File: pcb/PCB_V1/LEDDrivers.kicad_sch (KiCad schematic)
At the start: 50 parts, among them J711 LED +/- (return isolated), J721 LED +/- (return isolated), J731 LED +/- (return isolated), Q711 CSD19534Q5A, Q721 CSD19538Q3A, U700 SN74LVC1G08DBVR, U710 AL8853S-13, U720 AL8853S-13

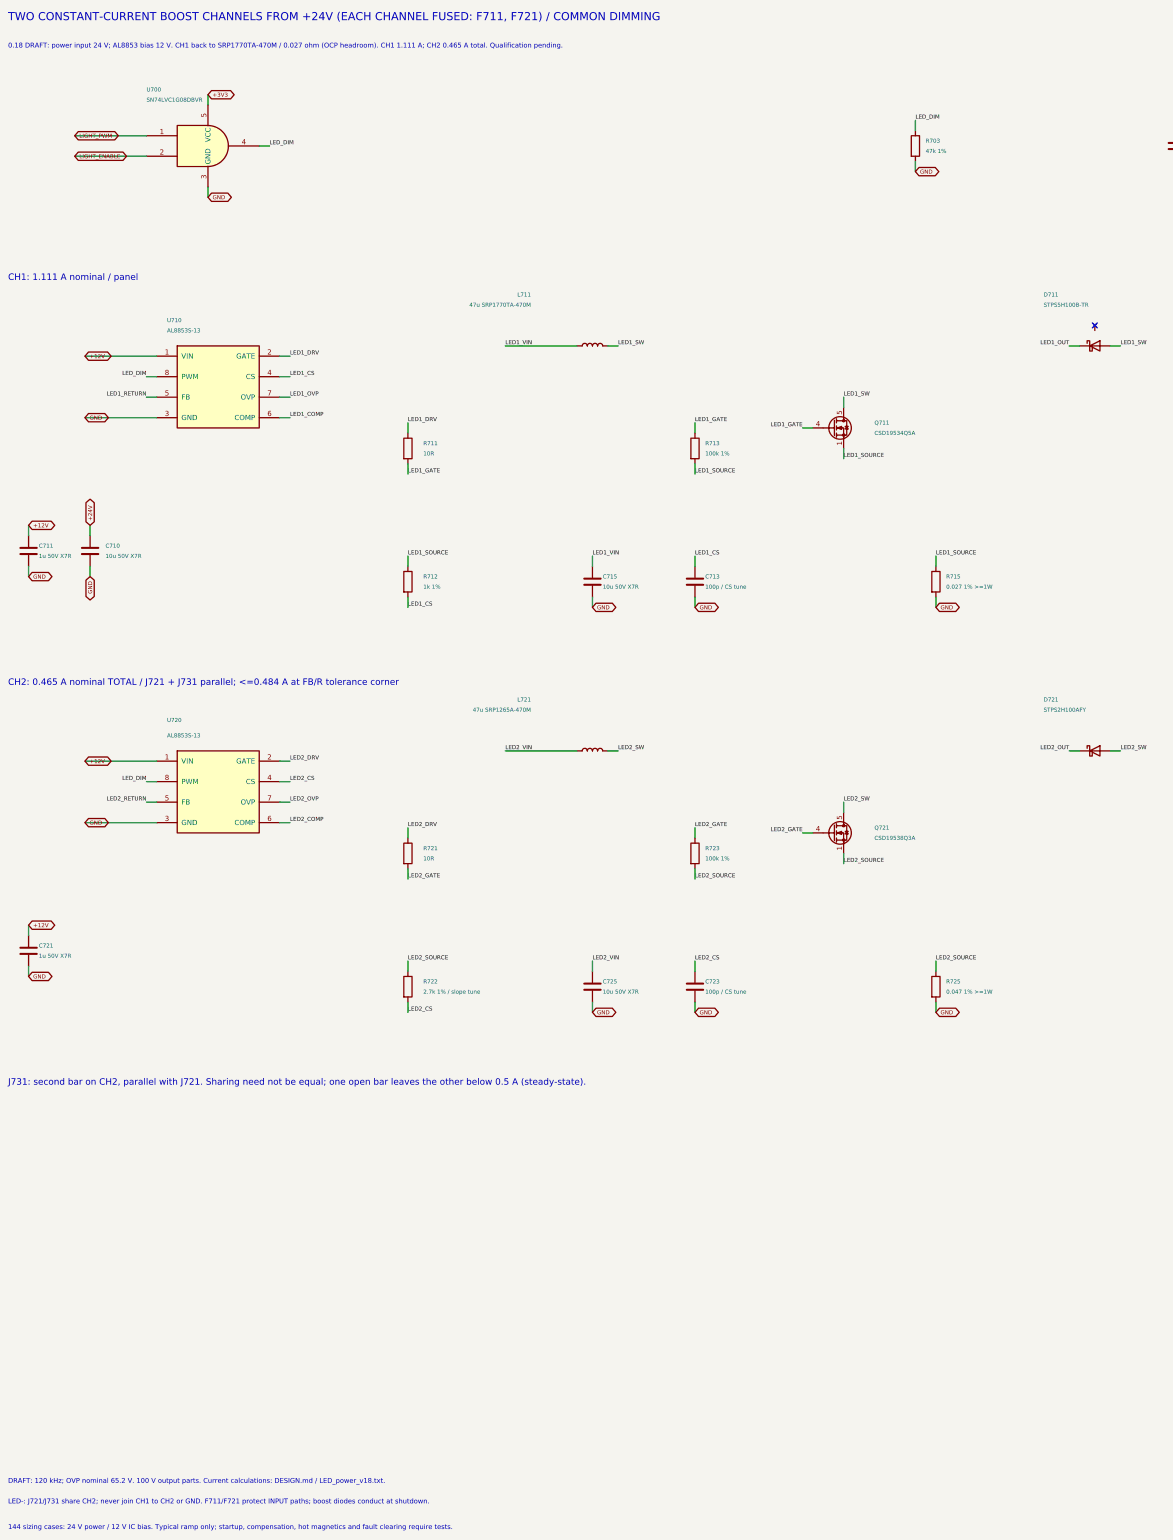
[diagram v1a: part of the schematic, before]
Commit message: pcb: revision 0.20 cost-down with new footprints and placement
- RTC: DS3231MZ replaced by NXP PCF8563T/5 with an Epson FC-135 crystal
  (CL 12.5 pF), C304 18 pF C0G on OSCI, BAT54C supply OR (D303) and R307
  1k from the CR2032.
- Boost switches Q711/Q721: AOS AOD66923 (DPAK) on a project footprint
  that keeps the S1/2/3 G4 D5 numbering; diodes D711/D721: Vishay SS5P10
  (TO-277A).
- L101 cjiang FXL0630-100-M and L902 PROD PSPMAA0604-220M-ANP on the
  KiCad FXL0630 land.
- LED switch areas and the RTC cluster re-placed (29 parts moved);
  ERC 0, DRC 0, 340 unrouted links.
- Checks, price/JLC snapshots v20, reports, placement images and docs
  updated: USD 31.62 per board (29.52 for five boards).

Co-Authored-By: Claude Opus 5.5 <noreply@anthropic.com>
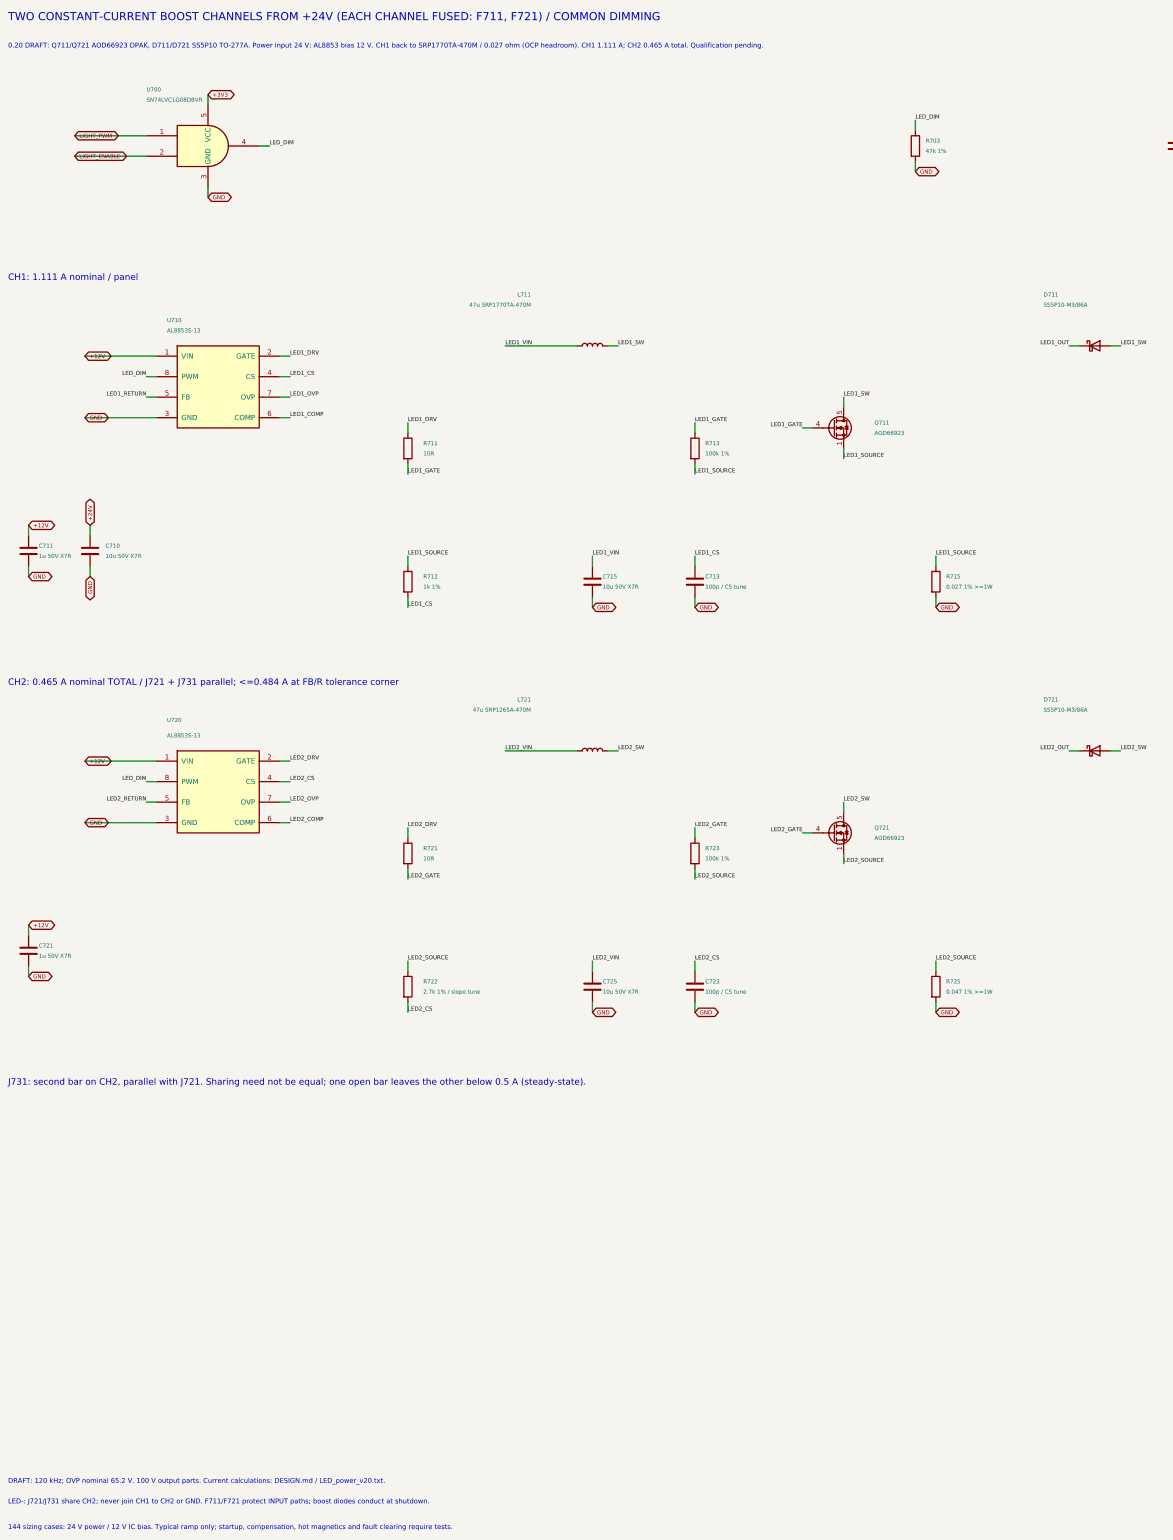
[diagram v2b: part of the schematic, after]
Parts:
- D711: value STPS5H100B-TR -> SS5P10-M3/86A; footprint Package_TO_SOT_SMD:TO-252-2 -> GrowBox:Vishay_TO-277A_D_K1_A2; symbol GrowBox:STPS5H100B -> Device:D_Schottky; LCSC C10648 -> C46986; MPN STPS5H100B-TR -> SS5P10-M3/86A; Manufacturer STMicroelectronics -> Vishay
- D721: value STPS2H100AFY -> SS5P10-M3/86A; footprint Diode_SMD:D_SOD-128 -> GrowBox:Vishay_TO-277A_D_K1_A2; LCSC C3757915 -> C46986; MPN STPS2H100AFY -> SS5P10-M3/86A; Manufacturer STMicroelectronics -> Vishay
- Q711: value CSD19534Q5A -> AOD66923; footprint GrowBox:TI_DQJ0008A_CSD19534Q5A -> GrowBox:TO-252-2_NMOS_S123_G4_D5; symbol GrowBox:CSD19534Q5A -> GrowBox:AOD66923; LCSC C114200 -> C485687; MPN CSD19534Q5A -> AOD66923; Manufacturer Texas Instruments -> AOS
- Q721: value CSD19538Q3A -> AOD66923; footprint GrowBox:TI_DNH0008A_CSD19538Q3A -> GrowBox:TO-252-2_NMOS_S123_G4_D5; symbol GrowBox:CSD19538Q3A -> GrowBox:AOD66923; LCSC (none) -> C485687; MPN (none) -> AOD66923; Manufacturer (none) -> AOS
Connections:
- net LED1_OUT: now also D711.1 (K); no longer D711.2 (K)
- net LED1_SW: now also D711.2 (A); no longer D711.3 (A)
- no-connect marks 1 -> 0
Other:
- note added: "0.20 DRAFT: Q711/Q721 AOD66923 DPAK, D711/D721 SS5P10 TO-277A. Power input 24 V; AL8853 bias 12 V. CH1 back to SRP1770TA-470M / 0.027 ohm (OCP headroom). CH1 1.111 A; CH2 0.465 A total. Qualification pending."
- note added: "DRAFT: 120 kHz; OVP nominal 65.2 V. 100 V output parts. Current calculations: DESIGN.md / LED_power_v20.txt."
- note removed: "0.18 DRAFT: power input 24 V; AL8853 bias 12 V. CH1 back to SRP1770TA-470M / 0.027 ohm (OCP headroom). CH1 1.111 A; CH2 0.465 A total. Qualification pending."
- note removed: "DRAFT: 120 kHz; OVP nominal 65.2 V. 100 V output parts. Current calculations: DESIGN.md / LED_power_v18.txt."
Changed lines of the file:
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@@
 		(title "07 - AL8853 LED drivers, 24 V input, 2 channels")
 		(date "2026-09-29")
-		(rev "0.18-DRAFT")
+		(rev "0.20-DRAFT")
 		(company "GrowBox controller")
 		(comment 1 "Simplified prototype; unrouted; hardware qualification pending")
@@
 		)
 	)
-	(text "DRAFT: 120 kHz; OVP nominal 65.2 V. 100 V output parts. Current calculations: DESIGN.md / LED_power_v18.txt."
+	(text "DRAFT: 120 kHz; OVP nominal 65.2 V. 100 V output parts. Current calculations: DESIGN.md / LED_power_v20.txt."
 		(exclude_from_sim no)
 		(at 20.32 378.46 0)
@@
 		)
 	)
-	(text "0.18 DRAFT: power input 24 V; AL8853 bias 12 V. CH1 back to SRP1770TA-470M / 0.027 ohm (OCP headroom). CH1 1.111 A; CH2 0.465 A total. Qualification pending."
+	(text "0.20 DRAFT: Q711/Q721 AOD66923 DPAK, D711/D721 SS5P10 TO-277A. Power input 24 V; AL8853 bias 12 V. CH1 back to SRP1770TA-470M / 0.027 ohm (OCP headroom). CH1 1.111 A; CH2 0.465 A total. Qualification pending."
 		(exclude_from_sim no)
 		(at 20.32 22.86 0)
@@
 			)
 		)
-		(property "Value" "STPS2H100AFY"
+		(property "Value" "SS5P10-M3/86A"
 			(at 276.86 187.96 0)
 			(show_name no)
@@
 			)
 		)
-		(property "Footprint" "Diode_SMD:D_SOD-128"
+		(property "Footprint" "GrowBox:Vishay_TO-277A_D_K1_A2"
 			(at 289.56 198.12 0)
 			(hide yes)
@@
 			)
 		)
-		(property "Datasheet" "https://www.st.com/resource/en/datasheet/stps2h100-y.pdf"
+		(property "Datasheet" "https://www.vishay.com/docs/88984/ss5p10.pdf"
 			(at 289.56 198.12 0)
 			(hide yes)
@@
 			)
 		)
-		(property "Manufacturer" "STMicroelectronics"
+		(property "Manufacturer" "Vishay"
 			(at 289.56 198.12 0)
 			(hide yes)
@@
 			)
 		)
-		(property "MPN" "STPS2H100AFY"
+		(property "MPN" "SS5P10-M3/86A"
 			(at 289.56 198.12 0)
 			(hide yes)
@@
 			)
 		)
-		(property "LCSC" "C3757915"
+		(property "LCSC" "C46986"
 			(at 289.56 198.12 0)
 			(hide yes)
@@
 	)
 	(symbol
-		(lib_id "GrowBox:STPS5H100B")
+		(lib_id "Device:D_Schottky")
 		(at 289.56 97.79 0)
 		(unit 1)
@@
 			)
 		)
-		(property "Value" "STPS5H100B-TR"
+		(property "Value" "SS5P10-M3/86A"
 			(at 276.86 87.63 0)
 			(show_name no)
@@
 			)
 		)
-		(property "Footprint" "Package_TO_SOT_SMD:TO-252-2"
+		(property "Footprint" "GrowBox:Vishay_TO-277A_D_K1_A2"
 			(at 289.56 97.79 0)
 			(hide yes)
@@
 			)
 		)
-		(property "Datasheet" "https://www.st.com/resource/en/datasheet/stps5h100.pdf"
+		(property "Datasheet" "https://www.vishay.com/docs/88984/ss5p10.pdf"
 			(at 289.56 97.79 0)
 			(hide yes)
@@
 			)
 		)
-		(property "Manufacturer" "STMicroelectronics"
+		(property "Manufacturer" "Vishay"
 			(at 289.56 97.79 0)
 			(hide yes)
@@
 			)
 		)
-		(property "MPN" "STPS5H100B-TR"
+		(property "MPN" "SS5P10-M3/86A"
 			(at 289.56 97.79 0)
 			(hide yes)
@@
 			)
 		)
-		(property "LCSC" "C10648"
+		(property "LCSC" "C46986"
 			(at 289.56 97.79 0)
 			(hide yes)
@@
 	)
 	(symbol
-		(lib_id "GrowBox:CSD19534Q5A")
+		(lib_id "GrowBox:AOD66923")
 		(at 224.79 118.11 0)
 		(unit 1)
@@
 			)
 		)
-		(property "Value" "CSD19534Q5A"
+		(property "Value" "AOD66923"
 			(at 234.95 119.38 0)
 			(show_name no)
@@
 			)
 		)
-		(property "Footprint" "GrowBox:TI_DQJ0008A_CSD19534Q5A"
+		(property "Footprint" "GrowBox:TO-252-2_NMOS_S123_G4_D5"
 			(at 224.79 118.11 0)
 			(hide yes)
@@
 			)
 		)
-		(property "Datasheet" ""
+		(property "Datasheet" "https://www.aosmd.com/res/datasheets/AOD66923.pdf"
 			(at 224.79 118.11 0)
 			(hide yes)
@@
 			)
 		)
-		(property "LCSC" "C114200"
+		(property "LCSC" "C485687"
 			(at 224.79 118.11 0)
 			(effects
@@
 			)
 		)
-		(property "MPN" "CSD19534Q5A"
+		(property "MPN" "AOD66923"
 			(at 224.79 118.11 0)
 			(effects
@@
 			)
 		)
-		(property "Manufacturer" "Texas Instruments"
+		(property "Manufacturer" "AOS"
 			(at 224.79 118.11 0)
 			(effects
@@
 	)
 	(symbol
-		(lib_id "GrowBox:CSD19538Q3A")
+		(lib_id "GrowBox:AOD66923")
 		(at 224.79 218.44 0)
 		(unit 1)
@@
 			)
 		)
-		(property "Value" "CSD19538Q3A"
+		(property "Value" "AOD66923"
 			(at 234.95 219.71 0)
 			(show_name no)
@@
 			)
 		)
-		(property "Footprint" "GrowBox:TI_DNH0008A_CSD19538Q3A"
+		(property "Footprint" "GrowBox:TO-252-2_NMOS_S123_G4_D5"
 			(at 224.79 218.44 0)
 			(hide yes)
@@
 			)
 		)
-		(property "Datasheet" "https://www.ti.com/lit/ds/symlink/csd19538q3a.pdf"
+		(property "Datasheet" "https://www.aosmd.com/res/datasheets/AOD66923.pdf"
 			(at 224.79 218.44 0)
 			(hide yes)
@@
 		(pin "5"
 		)
+		(property "Manufacturer" "AOS"
+			(at 224.79 218.44 0)
+			(effects
+				(font
+					(size 1 1)
+				)
+				(hide yes)
+				(justify left)
+			)
+		)
+		(property "LCSC" "C485687"
+			(at 224.79 218.44 0)
+			(effects
+				(font
+					(size 1 1)
+				)
+				(hide yes)
+				(justify left)
+			)
+		)
+		(property "MPN" "AOD66923"
+			(at 224.79 218.44 0)
+			(effects
+				(font
+					(size 1 1)
+				)
+				(hide yes)
+				(justify left)
+			)
+		)
 	)
 	(symbol
@@
 		)
 	)
-	(no_connect
-		(at 289.56 92.71)
-	)
 	(symbol
